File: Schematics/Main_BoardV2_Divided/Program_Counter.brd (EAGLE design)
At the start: 132.1 x 117.8 mm, 46 parts

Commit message: Routd and Cams Created
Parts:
- moved SV21 11.7 mm to (11.4, 49.5)
- moved PROGRAM-COUNTER1:IC3 10.5 mm to (47.0, 83.8)
- moved PROGRAM-COUNTER1:IC1 10.5 mm to (63.5, 109.2)
- moved PROGRAM-COUNTER1:IC2 10.5 mm to (63.5, 82.5)
- moved PROGRAM-COUNTER1:IC4 10.5 mm to (30.5, 82.5)
- moved PROGRAM-COUNTER1:IC5 10.5 mm to (30.5, 109.2)
- moved PROGRAM-COUNTER1:V1 10.5 mm to (30.5, 26.7)
- moved PROGRAM-COUNTER1:V4 10.5 mm to (30.5, 53.3)
- moved SV26 10.5 mm to (10.2, 78.7)
- moved JP21 10.5 mm to (10.2, 88.9)
- moved SV15 10.5 mm to (10.2, 108.0)
- moved SV25 10.5 mm to (10.2, 67.3)
- moved PROGRAM-COUNTER1:V2 10.5 mm to (54.6, 26.7)
- moved PROGRAM-COUNTER1:V3 10.5 mm to (54.6, 53.3)
- moved PROGRAM-COUNTER1:LED1 6.84 mm to (99.1, 118.1)
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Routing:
- net PROGRAM-COUNTER1:N$8: track 0.00 -> 207.9 mm, vias 0 -> 3
- net CLK: track 0.00 -> 196.6 mm
- net PROGRAM-COUNTER1:N$28: track 0.00 -> 194.4 mm, vias 0 -> 2
- net PROGRAM-COUNTER1:N$27: track 0.00 -> 187.6 mm, vias 0 -> 4
- net PROGRAM-COUNTER1:N$6: track 0.00 -> 174.0 mm, vias 0 -> 1
- net PROGRAM-COUNTER1:N$1: track 0.00 -> 171.9 mm, vias 0 -> 2
- net PROGRAM-COUNTER1:N$25: track 0.00 -> 170.1 mm, vias 0 -> 4
- net PROGRAM-COUNTER1:N$7: track 0.00 -> 158.5 mm, vias 0 -> 3
- net PROGRAM-COUNTER1:N$26: track 0.00 -> 157.5 mm, vias 0 -> 5
- net PROGRAM-COUNTER1:N$18: track 0.00 -> 142.7 mm, vias 0 -> 2
- net PC_LE: track 0.00 -> 137.6 mm, vias 0 -> 2
- net PROGRAM-COUNTER1:N$17: track 0.00 -> 135.4 mm, vias 0 -> 1
- net COUNT: track 0.00 -> 133.4 mm
- net CLR: track 0.00 -> 132.4 mm, vias 0 -> 1
- net PROGRAM-COUNTER1:N$5: track 0.00 -> 127.8 mm, vias 0 -> 1
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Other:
- board size 132.1 x 117.8 mm -> 105.4 x 117.8 mm
- board text added: "16Bit Bus"
- board text added: "8Bit Bus"
- board text added: "Address"
- board text added: "Control Signals"

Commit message: Visual Improvments
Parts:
- SV15: device con-lstb:MA08-1 -> pinhead:1X08
- SV21: device con-lstb:MA08-2 -> pinhead:2X08
- SV25, SV26: device con-lstb:MA03-1 -> pinhead:1X03
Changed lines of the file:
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@@
 <drawing>
 <settings>
-<setting alwaysvectorfont="no"/>
+<setting alwaysvectorfont="yes"/>
 <setting verticaltext="up"/>
 </settings>
@@
 </layers>
 <board>
-<fusionsync huburn="a.cGVyc29uYWw6dWUyYzAxZDJj" projecturn="a.cGVyc29uYWw6dWUyYzAxZDJjIzIwMTkwNTA1MTkyMDg5NTI2" f3durn="urn:adsk.wipprod:dm.lineage:9ladLIGWRumA9Web2DwhSg" pcbguid="19dfac47-98ce-4076-aa97-989377772107" lastpulledtime="" lastsyncedchangeguid="5d790192-6e58-6aeb-05a2-1ad9496661d5"/>
+<fusionsync huburn="a.cGVyc29uYWw6dWUyYzAxZDJj" projecturn="a.cGVyc29uYWw6dWUyYzAxZDJjIzIwMTkwNTA1MTkyMDg5NTI2" f3durn="urn:adsk.wipprod:dm.lineage:9ladLIGWRumA9Web2DwhSg" pcbguid="19dfac47-98ce-4076-aa97-989377772107" lastpulledtime="" lastsyncedchangeguid="4ac1a1ea-363e-2df0-23d8-2de26f76d1e8"/>
 <plain>
 <wire x1="3.81" y1="7.62" x2="109.2" y2="7.62" width="0" layer="20"/>
@@
 <attribute name="VALUE" x="30.48" y="53.34" size="1.27" layer="27" ratio="10" rot="R270"/>
 </element>
-<element name="SV15" library="con-lstb" library_urn="urn:adsk.eagle:library:162" package="MA08-1" package3d_urn="urn:adsk.eagle:package:8343/1" value="" x="10.16" y="107.95" smashed="yes" rot="R270">
+<element name="SV15" library="pinhead" library_urn="urn:adsk.eagle:library:325" package="1X08" package3d_urn="urn:adsk.eagle:package:22409/2" value="" x="10.16" y="107.95" smashed="yes" rot="R270">
 <attribute name="MF" value="" x="10.16" y="107.95" size="1.778" layer="27" rot="R270" display="off"/>
 <attribute name="MPN" value="" x="10.16" y="107.95" size="1.778" layer="27" rot="R270" display="off"/>
@@
 <attribute name="VALUE" x="10.16" y="107.95" size="1.27" layer="27" ratio="10" rot="R270"/>
 </element>
-<element name="SV21" library="con-lstb" library_urn="urn:adsk.eagle:library:162" package="MA08-2" package3d_urn="urn:adsk.eagle:package:8335/1" value="" x="11.43" y="49.53" smashed="yes" rot="R270">
+<element name="SV21" library="pinhead" library_urn="urn:adsk.eagle:library:325" package="2X08" package3d_urn="urn:adsk.eagle:package:22481/2" value="" x="11.43" y="49.53" smashed="yes" rot="R270">
 <attribute name="MF" value="" x="11.43" y="49.53" size="1.778" layer="27" rot="R270" display="off"/>
 <attribute name="MPN" value="" x="11.43" y="49.53" size="1.778" layer="27" rot="R270" display="off"/>
@@
 <attribute name="VALUE" x="11.43" y="49.53" size="1.27" layer="27" ratio="10" rot="R270"/>
 </element>
-<element name="SV25" library="con-lstb" library_urn="urn:adsk.eagle:library:162" package="MA03-1" package3d_urn="urn:adsk.eagle:package:8339/1" value="" x="10.16" y="67.31" smashed="yes" rot="R270">
+<element name="SV25" library="pinhead" library_urn="urn:adsk.eagle:library:325" package="1X03" package3d_urn="urn:adsk.eagle:package:22458/2" value="" x="10.16" y="67.31" smashed="yes" rot="R270">
 <attribute name="MF" value="" x="10.16" y="67.31" size="1.778" layer="27" rot="R270" display="off"/>
 <attribute name="MPN" value="" x="10.16" y="67.31" size="1.778" layer="27" rot="R270" display="off"/>
@@
 <attribute name="VALUE" x="7.239" y="71.12" size="1.27" layer="27" ratio="10" rot="R270"/>
 </element>
-<element name="SV26" library="con-lstb" library_urn="urn:adsk.eagle:library:162" package="MA03-1" package3d_urn="urn:adsk.eagle:package:8339/1" value="" x="10.16" y="78.74" smashed="yes" rot="R270">
+<element name="SV26" library="pinhead" library_urn="urn:adsk.eagle:library:325" package="1X03" package3d_urn="urn:adsk.eagle:package:22458/2" value="" x="10.16" y="78.74" smashed="yes" rot="R270">
 <attribute name="MF" value="" x="10.16" y="78.74" size="1.778" layer="27" rot="R270" display="off"/>
 <attribute name="MPN" value="" x="10.16" y="78.74" size="1.778" layer="27" rot="R270" display="off"/>

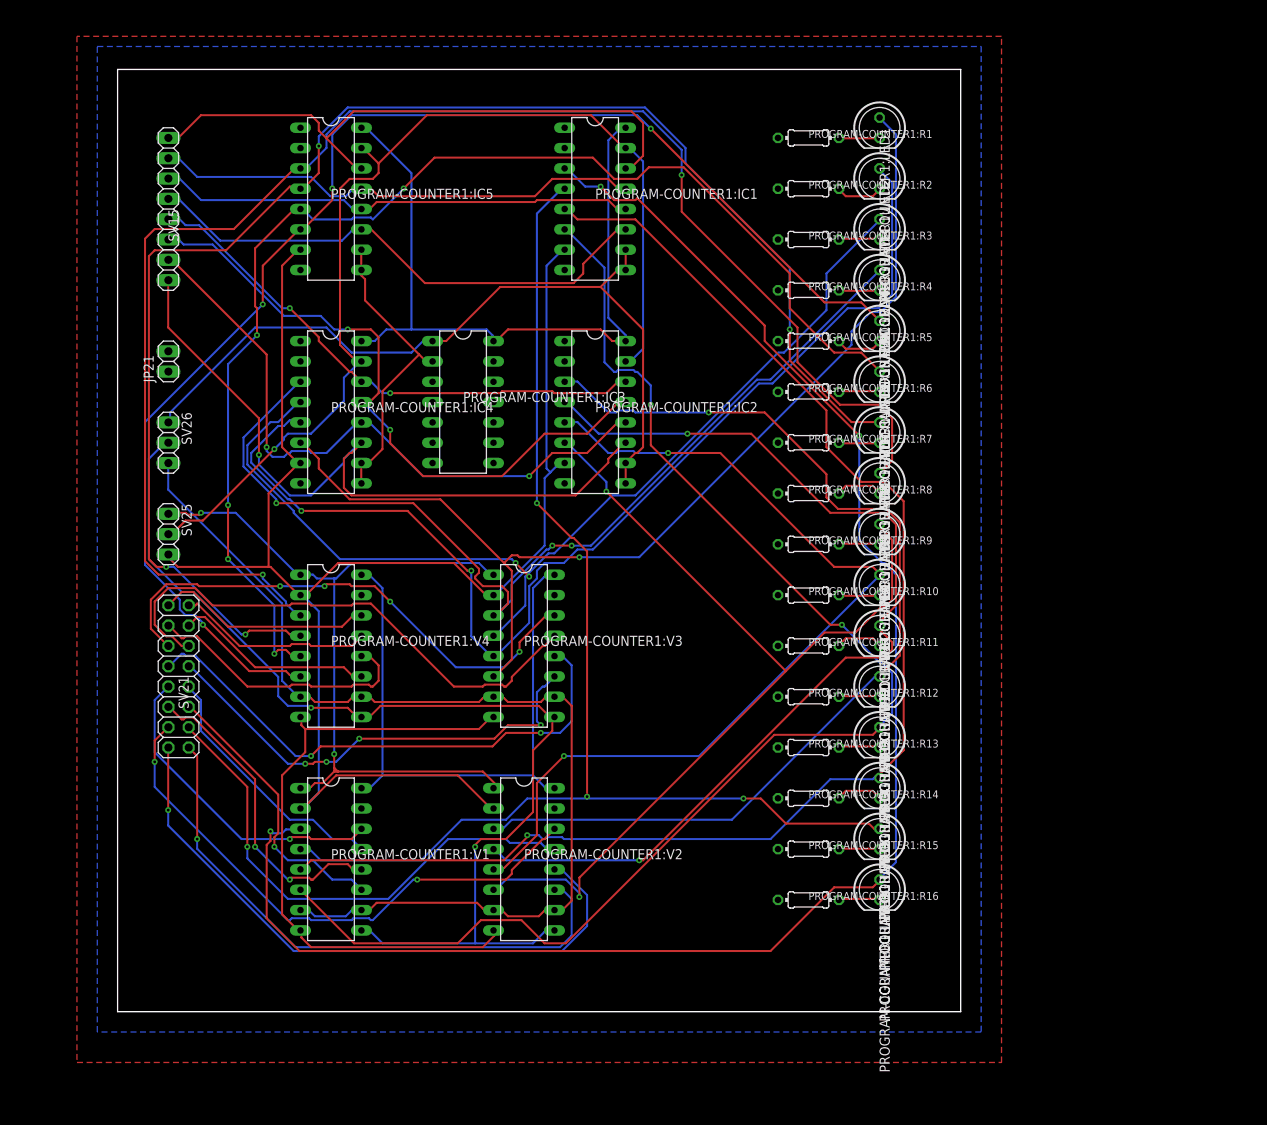
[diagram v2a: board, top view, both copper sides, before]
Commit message: Microcode Added and Ram Updated
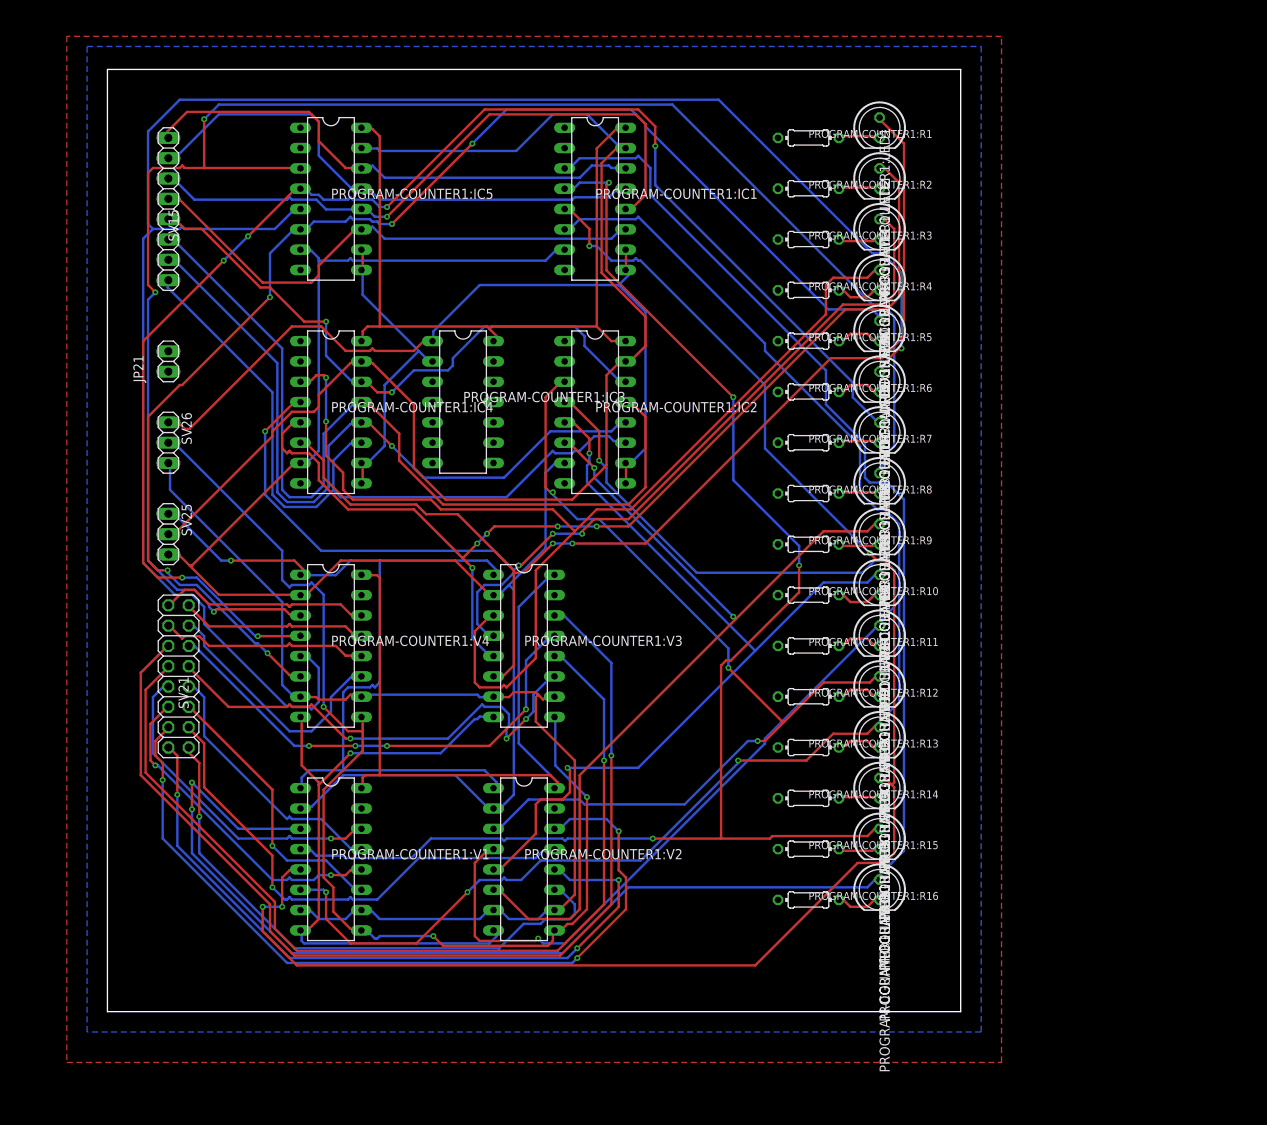
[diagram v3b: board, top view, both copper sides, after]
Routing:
- net PROGRAM-COUNTER1:N$26: track 157.5 -> 231.5 mm, vias 5 -> 1
- net N$5: track 66.0 -> 130.2 mm, vias 4 -> 1
- net N$7: track 67.7 -> 119.7 mm, vias 2 -> 1
- net N$13: track 70.5 -> 101.6 mm, vias 2 -> 3
- net 8B_6: track 82.5 -> 112.2 mm, vias 2 -> 0
- net CLR: track 132.4 -> 161.9 mm, vias 1 -> 0
- net PROGRAM-COUNTER1:N$8: track 207.9 -> 237.3 mm, vias 3 -> 2
- net PROGRAM-COUNTER1:N$6: track 174.0 -> 202.0 mm, vias 1 -> 4
- net PROGRAM-COUNTER1:N$28: track 194.4 -> 215.5 mm, vias 2 -> 3
- net 8B_3: track 59.7 -> 79.9 mm, vias 0 -> 1
- net PROGRAM-COUNTER1:N$7: track 158.5 -> 177.3 mm, vias 3 -> 4
- net PROGRAM-COUNTER1:N$4: track 126.2 -> 143.1 mm
- net PROGRAM-COUNTER1:N$20: track 126.2 -> 140.5 mm, vias 3 -> 2
- net PROGRAM-COUNTER1:N$5: track 127.8 -> 114.8 mm, vias 1 -> 3
- net 8B_1: track 77.3 -> 65.0 mm
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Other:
- board size 105.4 x 117.8 mm -> 106.7 x 117.8 mm
